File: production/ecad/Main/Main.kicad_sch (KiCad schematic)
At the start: 1 part, among them J1 61204021621

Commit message: merged david and neha work
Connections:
- net W_DAT: now reaches J1.13
- net W_SCK: now reaches J1.7
- net 3.3v renamed +3.3V
- net 5v renamed +5V
- net BMS/GND: no longer names the net of J1.36
- no-connect marks 13 -> 9
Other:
- added sheet Load_Cell_and_Amplifier (../LOAD-CELL/LOAD-CELL.kicad_sch)
- sheet ANO Dial: file ../Peripheral/Peripheral.kicad_sch -> ../ANO-DIAL/ANO-DIAL.kicad_sch

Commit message: Stylistic edits made
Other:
- note added: "Still need: - weight sensor - ADC (maybe)"
- note removed: "Still need: - weight sensor - ADC (maybe) -"
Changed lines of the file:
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@@
 	(wire
 		(pts
-			(xy 203.2 53.34) (xy 209.55 53.34)
+			(xy 204.47 53.34) (xy 209.55 53.34)
 		)
 		(stroke
@@
 	(polyline
 		(pts
-			(xy 181.61 96.52) (xy 181.61 26.67)
+			(xy 186.69 96.52) (xy 186.69 26.67)
 		)
 		(stroke
@@
 	(wire
 		(pts
-			(xy 120.65 129.54) (xy 124.46 129.54)
+			(xy 120.65 129.54) (xy 125.73 129.54)
 		)
 		(stroke
@@
 	(polyline
 		(pts
-			(xy 120.65 96.52) (xy 181.61 96.52)
+			(xy 120.65 96.52) (xy 186.69 96.52)
 		)
 		(stroke
@@
 	(polyline
 		(pts
-			(xy 118.11 26.67) (xy 118.11 96.52)
+			(xy 106.68 26.67) (xy 106.68 96.52)
 		)
 		(stroke
@@
 	(polyline
 		(pts
-			(xy 118.11 26.67) (xy 180.34 26.67)
+			(xy 106.68 26.67) (xy 180.34 26.67)
 		)
 		(stroke
@@
 	(polyline
 		(pts
-			(xy 181.61 26.67) (xy 180.34 26.67)
+			(xy 186.69 26.67) (xy 180.34 26.67)
 		)
 		(stroke
@@
 	(polyline
 		(pts
-			(xy 118.11 96.52) (xy 120.65 96.52)
+			(xy 106.68 96.52) (xy 120.65 96.52)
 		)
 		(stroke
@@
 	(wire
 		(pts
-			(xy 201.93 57.15) (xy 209.55 57.15)
-		)
-		(stroke
-			(width 0)
-			(type default)
-		)
-	)
-	(text "Still need:\n- weight sensor\n- ADC (maybe)\n- "
+			(xy 204.47 57.15) (xy 209.55 57.15)
+		)
+		(stroke
+			(width 0)
+			(type default)
+		)
+	)
+	(text "Still need:\n- weight sensor\n- ADC (maybe)"
 		(exclude_from_sim no)
 		(at 157.226 20.32 0)
@@
 				(size 1.27 1.27)
 			)
+			(justify left)
 		)
 	)
 	(text "Raspberry Pi W Zero 2 Pins"
 		(exclude_from_sim no)
-		(at 146.304 30.988 0)
+		(at 146.304 29.972 0)
 		(effects
 			(font
@@
 				(size 1.27 1.27)
 			)
+			(justify left)
 		)
 	)
@@
 	(global_label "ANO_SW2"
 		(shape input)
-		(at 203.2 53.34 180)
+		(at 204.47 53.34 180)
 		(fields_autoplaced yes)
 		(effects
@@
 		)
 		(property "Intersheetrefs" "${INTERSHEET_REFS}"
-			(at 191.6272 53.34 0)
+			(at 192.8972 53.34 0)
 			(effects
 				(font
@@
 	(global_label "ANO_SW3"
 		(shape input)
-		(at 201.93 57.15 180)
+		(at 204.47 57.15 180)
 		(fields_autoplaced yes)
 		(effects
@@
 		)
 		(property "Intersheetrefs" "${INTERSHEET_REFS}"
-			(at 190.3572 57.15 0)
+			(at 192.8972 57.15 0)
 			(effects
 				(font
@@
 	(global_label "3V3EXT"
 		(shape input)
-		(at 124.46 129.54 0)
+		(at 125.73 129.54 0)
 		(fields_autoplaced yes)
 		(effects
@@
 		)
 		(property "Intersheetrefs" "${INTERSHEET_REFS}"
-			(at 134.2789 129.54 0)
-			(effects
-				(font
+			(at 135.5489 129.54 0)
+			(effects
+				(font

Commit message: more changes
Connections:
- net GND: no longer J1.20
- net MTR_IN1: no longer J1.33
- net MISO: no longer names the net of J1.21
- net SCL: no longer names the net of J1.5
- net SDA: no longer names the net of J1.3

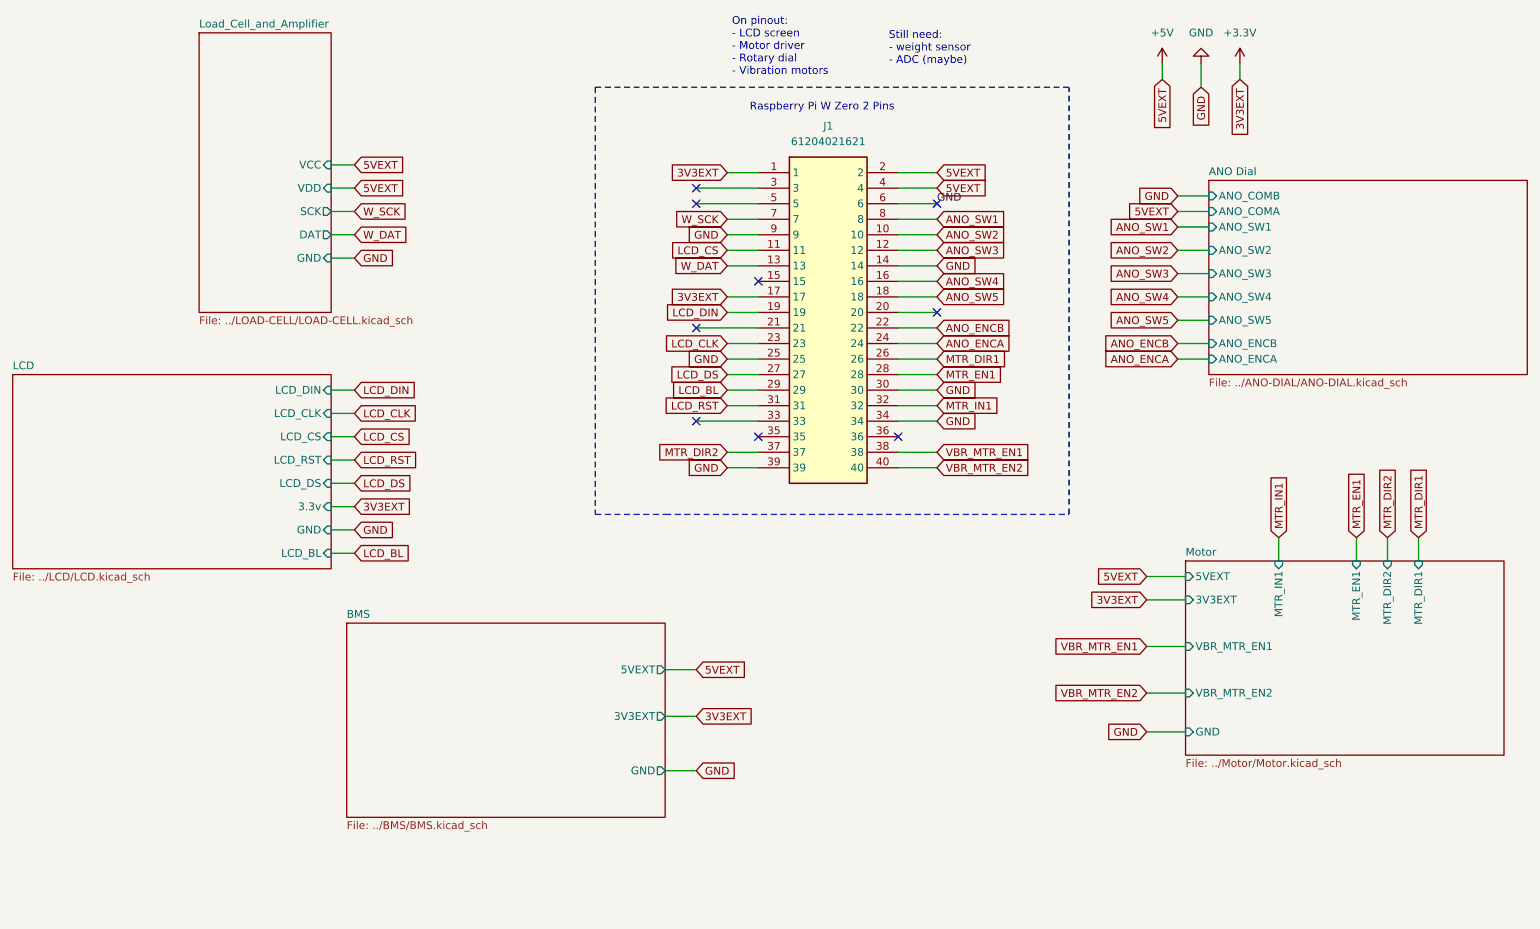
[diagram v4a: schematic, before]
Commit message: changed pinout
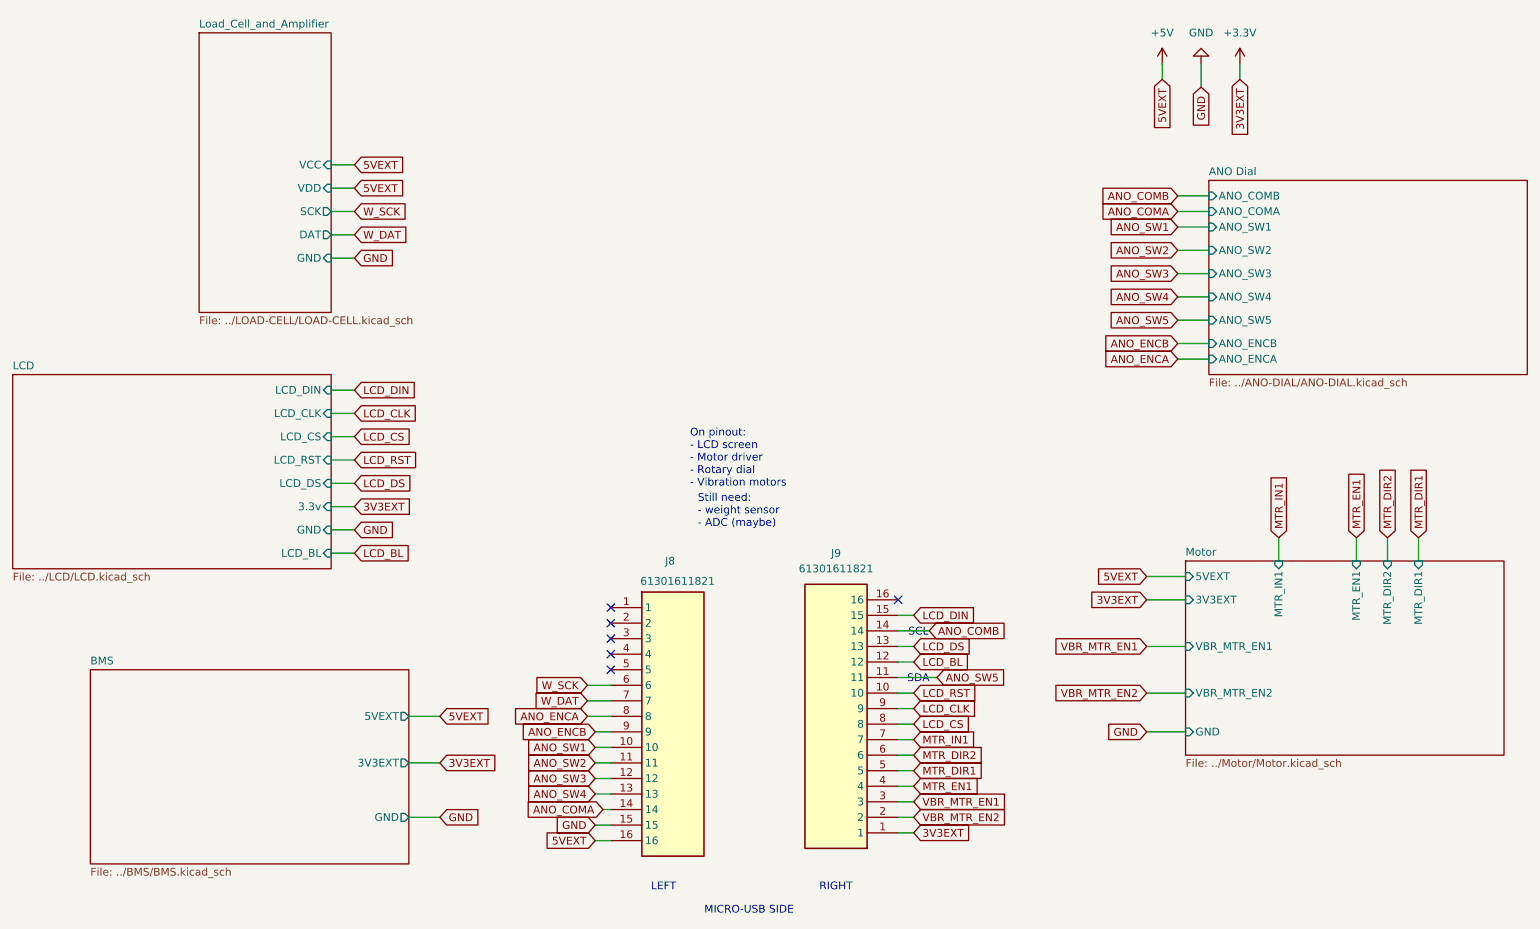
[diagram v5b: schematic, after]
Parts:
- removed J1: 61204021621, SHDR40W79P254X254_2X20_5846X910X925P, symbol Headers:61204021621
- added J8, J9: 61301611821, RHDR16W82P0X254_1X16_4114X250X865P, symbol 16positionheader:61301611821
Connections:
- net +3.3V: now also J9.1
- net +5V: now also J8.16
- net ANO_ENCA: now also J8.8
- net ANO_ENCB: now also J8.9
- net ANO_SW1: now also J8.10
- net ANO_SW2: now also J8.11
- net ANO_SW3: now also J8.12
- net ANO_SW4: now also J8.13
- net ANO_SW5: now also J9.11
- net GND: now also J8.15
- net LCD_BL: now also J9.12
- net LCD_CLK: now also J9.9
- net LCD_CS: now also J9.8
- net LCD_DIN: now also J9.15
- net LCD_DS: now also J9.13
- net LCD_RST: now also J9.10
- net MTR_DIR1: now also J9.5
- net MTR_DIR2: now also J9.6
- net MTR_EN1: now also J9.4
- net MTR_IN1: now also J9.7
- net VBR_MTR_EN1: now also J9.3
- net VBR_MTR_EN2: now also J9.2
- net W_DAT: now also J8.7
- net W_SCK: now also J8.6
- new net ANO_COMA: J8.14
- new net ANO_COMB: J9.14
- no-connect marks 9 -> 6
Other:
- note added: "LEFT"
- note added: "MICRO-USB SIDE"
- note added: "RIGHT"
- note added: "SCL"
- note added: "SDA"
- note removed: "Raspberry Pi W Zero 2 Pins"

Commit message: note
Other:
- note added: "ANO_DIAL may need I2C lines, so either we have multiple slaves or give up the bus for the BMS SOC"
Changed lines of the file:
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@@
+		)
+	)
+	(text "ANO_DIAL may need I2C lines, so either we have multiple slaves or give up the bus for the BMS SOC"
+		(exclude_from_sim no)
+		(at 139.446 102.362 0)
+		(effects
+			(font
+				(size 1.27 1.27)
+			)
 		)
 	)

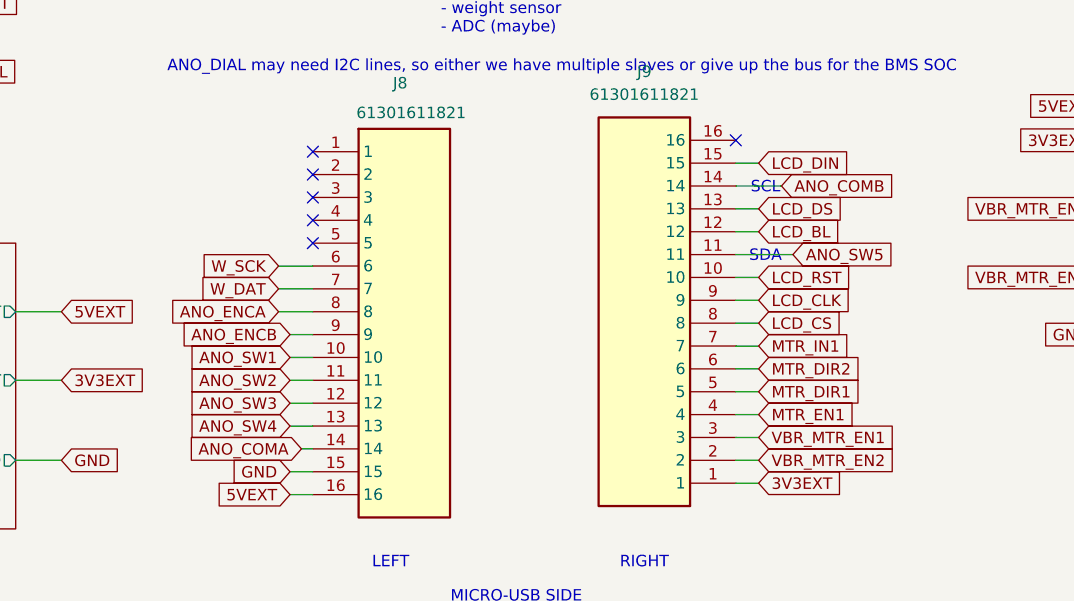
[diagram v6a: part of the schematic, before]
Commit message: reverted to Max branch from Wed and moved ANO button GPIO pins to input only
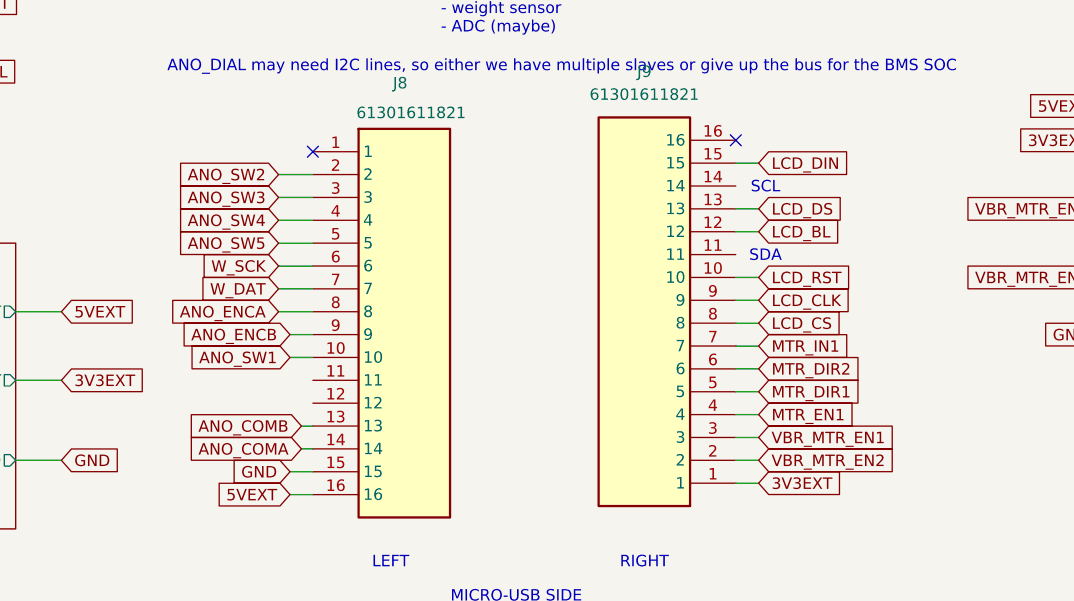
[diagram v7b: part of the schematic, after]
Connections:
- net ANO_COMB: now also J8.13; no longer J9.14
- net ANO_SW2: now also J8.2; no longer J8.11
- net ANO_SW3: now also J8.3; no longer J8.12
- net ANO_SW4: now also J8.4; no longer J8.13
- net ANO_SW5: now also J8.5; no longer J9.11
- no-connect marks 6 -> 2
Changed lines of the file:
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@@
 	(paper "A4")
 	(no_connect
-		(at 111.76 119.38)
-	)
-	(no_connect
-		(at 111.76 116.84)
-	)
-	(no_connect
 		(at 111.76 111.76)
-	)
-	(no_connect
-		(at 111.76 121.92)
 	)
 	(no_connect
 		(at 158.75 110.49)
 	)
-	(no_connect
-		(at 111.76 114.3)
-	)
 	(wire
 		(pts
@@
 	(wire
 		(pts
-			(xy 109.22 137.16) (xy 111.76 137.16)
-		)
-		(stroke
-			(width 0)
-			(type default)
-		)
-	)
-	(wire
-		(pts
 			(xy 158.75 148.59) (xy 161.29 148.59)
 		)
@@
 	(wire
 		(pts
-			(xy 109.22 142.24) (xy 111.76 142.24)
+			(xy 107.95 119.38) (xy 111.76 119.38)
 		)
 		(stroke
@@
 	(wire
 		(pts
+			(xy 110.49 142.24) (xy 111.76 142.24)
+		)
+		(stroke
+			(width 0)
+			(type default)
+		)
+	)
+	(wire
+		(pts
 			(xy 243.84 100.33) (xy 243.84 104.14)
 		)
@@
 	(wire
 		(pts
+			(xy 107.95 114.3) (xy 111.76 114.3)
+		)
+		(stroke
+			(width 0)
+			(type default)
+		)
+	)
+	(wire
+		(pts
 			(xy 66.04 54.61) (xy 69.85 54.61)
 		)
@@
 	(wire
 		(pts
-			(xy 109.22 139.7) (xy 111.76 139.7)
-		)
-		(stroke
-			(width 0)
-			(type default)
-		)
-	)
-	(wire
-		(pts
 			(xy 220.98 100.33) (xy 220.98 104.14)
 		)
@@
 	(wire
 		(pts
-			(xy 158.75 115.57) (xy 163.83 115.57)
-		)
-		(stroke
-			(width 0)
-			(type default)
-		)
-	)
-	(wire
-		(pts
-			(xy 158.75 123.19) (xy 165.1 123.19)
-		)
-		(stroke
-			(width 0)
-			(type default)
-		)
-	)
-	(wire
-		(pts
 			(xy 204.47 44.45) (xy 209.55 44.45)
 		)
@@
 	(wire
 		(pts
+			(xy 107.95 116.84) (xy 111.76 116.84)
+		)
+		(stroke
+			(width 0)
+			(type default)
+		)
+	)
+	(wire
+		(pts
 			(xy 204.47 60.96) (xy 209.55 60.96)
 		)
@@
 		(pts
 			(xy 201.93 22.86) (xy 201.93 25.4)
+		)
+		(stroke
+			(width 0)
+			(type default)
+		)
+	)
+	(wire
+		(pts
+			(xy 107.95 121.92) (xy 111.76 121.92)
 		)
 		(stroke
@@
 	(global_label "ANO_SW5"
 		(shape input)
-		(at 165.1 123.19 0)
-		(fields_autoplaced yes)
-		(effects
-			(font
-				(size 1.27 1.27)
-			)
-			(justify left)
-		)
-		(property "Intersheetrefs" "${INTERSHEET_REFS}"
-			(at 176.6728 123.19 0)
-			(effects
-				(font
-					(size 1.27 1.27)
-				)
-				(justify left)
+		(at 107.95 121.92 180)
+		(fields_autoplaced yes)
+		(effects
+			(font
+				(size 1.27 1.27)
+			)
+			(justify right)
+		)
+		(property "Intersheetrefs" "${INTERSHEET_REFS}"
+			(at 96.3772 121.92 0)
+			(effects
+				(font
+					(size 1.27 1.27)
+				)
+				(justify right)
 				(hide yes)
 			)
@@
 	(global_label "ANO_COMB"
 		(shape input)
-		(at 163.83 115.57 0)
-		(fields_autoplaced yes)
-		(effects
-			(font
-				(size 1.27 1.27)
-			)
-			(justify left)
-		)
-		(property "Intersheetrefs" "${INTERSHEET_REFS}"
-			(at 176.8543 115.57 0)
-			(effects
-				(font
-					(size 1.27 1.27)
-				)
-				(justify left)
+		(at 110.49 142.24 180)
+		(fields_autoplaced yes)
+		(effects
+			(font
+				(size 1.27 1.27)
+			)
+			(justify right)
+		)
+		(property "Intersheetrefs" "${INTERSHEET_REFS}"
+			(at 97.4657 142.24 0)
+			(effects
+				(font
+					(size 1.27 1.27)
+				)
+				(justify right)
 				(hide yes)
 			)
@@
 	(global_label "ANO_SW3"
 		(shape input)
-		(at 109.22 139.7 180)
-		(fields_autoplaced yes)
-		(effects
-			(font
-				(size 1.27 1.27)
-			)
-			(justify right)
-		)
-		(property "Intersheetrefs" "${INTERSHEET_REFS}"
-			(at 97.6472 139.7 0)
+		(at 107.95 116.84 180)
+		(fields_autoplaced yes)
+		(effects
+			(font
+				(size 1.27 1.27)
+			)
+			(justify right)
+		)
+		(property "Intersheetrefs" "${INTERSHEET_REFS}"
+			(at 96.3772 116.84 0)
 			(effects
 				(font
@@
 	(global_label "ANO_SW2"
 		(shape input)
-		(at 109.22 137.16 180)
-		(fields_autoplaced yes)
-		(effects
-			(font
-				(size 1.27 1.27)
-			)
-			(justify right)
-		)
-		(property "Intersheetrefs" "${INTERSHEET_REFS}"
-			(at 97.6472 137.16 0)
+		(at 107.95 114.3 180)
+		(fields_autoplaced yes)
+		(effects
+			(font
+				(size 1.27 1.27)
+			)
+			(justify right)
+		)
+		(property "Intersheetrefs" "${INTERSHEET_REFS}"
+			(at 96.3772 114.3 0)
 			(effects
 				(font
@@
 	(global_label "ANO_SW4"
 		(shape input)
-		(at 109.22 142.24 180)
-		(fields_autoplaced yes)
-		(effects
-			(font
-				(size 1.27 1.27)
-			)
-			(justify right)
-		)
-		(property "Intersheetrefs" "${INTERSHEET_REFS}"
-			(at 97.6472 142.24 0)
-			(effects
-				(font
+		(at 107.95 119.38 180)
+		(fields_autoplaced yes)
+		(effects
+			(font
+				(size 1.27 1.27)
+			)
+			(justify right)
+		)
+		(property "Intersheetrefs" "${INTERSHEET_REFS}"
+			(at 96.3772 119.38 0)
+			(effects
+				(font
